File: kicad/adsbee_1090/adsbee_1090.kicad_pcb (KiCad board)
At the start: 4 copper layers, 33.5 x 30 mm, 84 parts, among them J1 U.FL 6GHz 50R, J2 USB_Micro-B_Receptacle, J3 Conn_02x03_Odd_Even, J4 Conn_ARM_JTAG_SWD_10, Q1 BSS84, SW1 SW_Push, SW2 SW_Push, SW3 SN74LVC1G3157, U1 AD8314, U2 BGA2818, U3 MCP6566, U4 AP2112K-3.3, U5 W25Q128JVS, U6 RP2040, U7 OPA358AIDCKR, X1 SF2321D, Y1 12.000MHz 18pF ±20ppm 80R

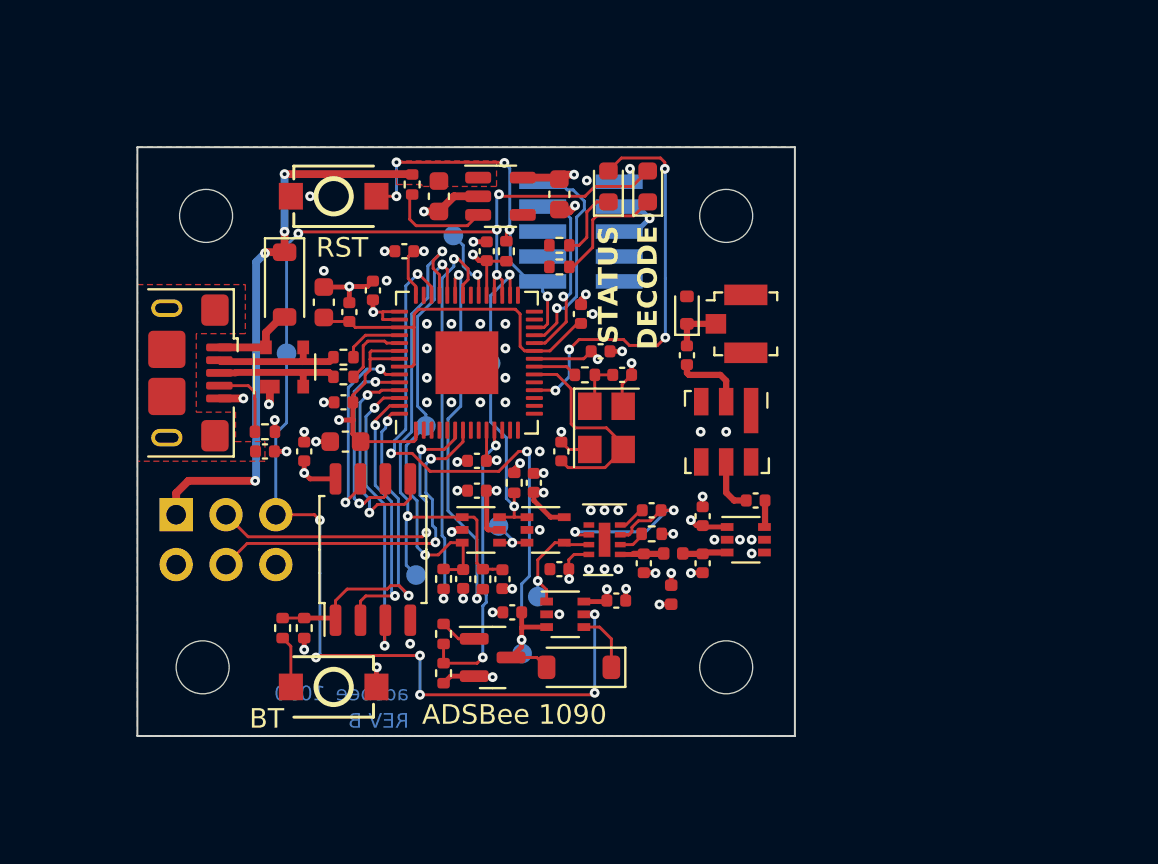
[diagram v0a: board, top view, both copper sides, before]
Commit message: Make ADSBee PCBA Rev C
* production folder for JLCPCB has U5 and X1 removed due to stockout.
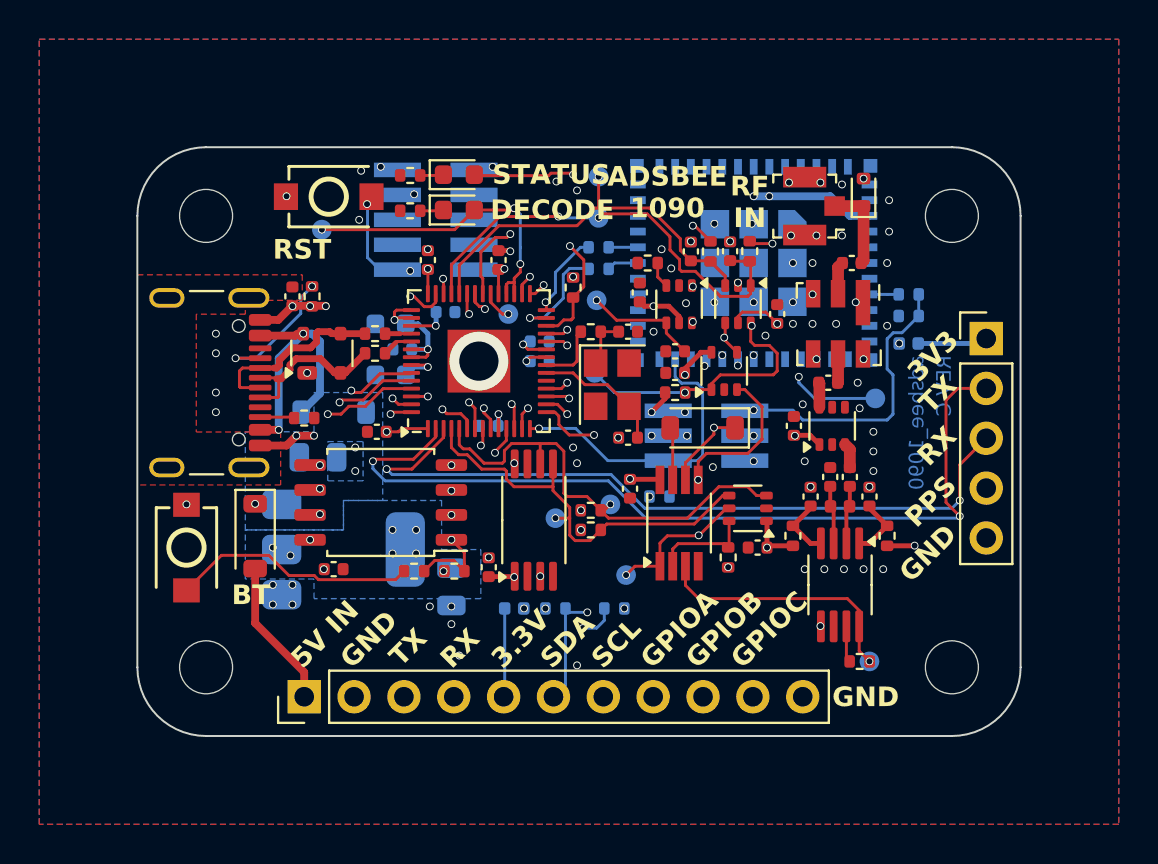
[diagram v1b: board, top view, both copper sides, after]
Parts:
- removed the C21 at (56.5, 37.9)
- removed the C27 at (60.8, 56.7)
- removed the C28 at (59.4, 58.6)
- removed the C8 at (61.2, 54.0)
- removed L2: 12nH, Inductor_SMD:L_0402_1005Metric
- removed Q1: BSS84, Package_TO_SOT_SMD:SOT-23
- removed the R13 at (49.0, 37.4)
- removed the R6 at (50.6, 60.3)
- removed the U1 at (58.8, 55.5)
- removed the U7 at (56.8, 59.3)
- added C10: 3pF, Capacitor_SMD:C_0402_1005Metric, F.Cu at (70.3, 52.3)
- added C13: 0.1uF, Capacitor_SMD:C_0402_1005Metric, F.Cu at (66.6, 55.9)
- added C14: 0.1uF, Capacitor_SMD:C_0402_1005Metric, F.Cu at (60.6, 42.9)
- added C32: 10uF, Capacitor_SMD:C_0805_2012Metric, B.Cu at (51.0, 57.9)
- added C4: 0.1uF, Capacitor_SMD:C_0402_1005Metric, F.Cu at (69.3, 53.3)
- added C6: 0.1uF, Capacitor_SMD:C_0402_1005Metric, F.Cu at (60.1, 52.9)
- added C9: 3pF, Capacitor_SMD:C_0402_1005Metric, F.Cu at (71.3, 52.3)
- added D6: 20V 1A, Diode_SMD:D_SOD-123, F.Cu at (41.0, 55.3)
- added F1: 6V 200mA, Fuse:Fuse_0402_1005Metric, B.Cu at (74.3, 45.5)
- added F2: 6V 200mA, Fuse:Fuse_0402_1005Metric, B.Cu at (54.2, 59.0)
- added J5: Conn_01x05_Pin, Connector_PinHeader_2.54mm:PinHeader_1x05_P2.54mm_Vertical, F.Cu at (78.2, 45.2)
- added J6: Conn_01x11_Pin, Connector_PinHeader_2.54mm:PinHeader_1x11_P2.54mm_Vertical, F.Cu at (43.5, 63.5)
- added R10: 5.1k, Resistor_SMD:R_0402_1005Metric, F.Cu at (43.5, 49.3)
- added R11: 2.2k, Resistor_SMD:R_0402_1005Metric, F.Cu at (58.1, 55.0)
- added R12: 2.2k, Resistor_SMD:R_0402_1005Metric, F.Cu at (58.1, 54.0)
- added R16: 2.2k, Resistor_SMD:R_0402_1005Metric, B.Cu at (56.3, 59.0)
- added R17: 2.2k, Resistor_SMD:R_0402_1005Metric, B.Cu at (59.3, 59.0)
- added R18: 0R, Resistor_SMD:R_0402_1005Metric, B.Cu at (74.3, 43.0)
- added R19: 0R, Resistor_SMD:R_0402_1005Metric, B.Cu at (58.5, 40.6)
- added R2: 10R, Resistor_SMD:R_0402_1005Metric, F.Cu at (73.2, 55.3)
- added R20: 0R, Resistor_SMD:R_0402_1005Metric, B.Cu at (58.5, 41.7)
- added R22: 10k, Resistor_SMD:R_0402_1005Metric, B.Cu at (61.6, 53.3)
- added R23: 10k, Resistor_SMD:R_0402_1005Metric, B.Cu at (74.3, 44.1)
- added R8: 20R, Resistor_SMD:R_0402_1005Metric, F.Cu at (61.0, 41.4)
- added R9: 5.1k, Resistor_SMD:R_0402_1005Metric, F.Cu at (43.9, 43.1)
- added SW2: SN74LVC1G3157, Package_TO_SOT_SMD:SOT-363_SC-70-6, F.Cu at (62.6, 43.5)
- added TP3: TestPoint, TestPoint:TestPoint_Pad_D1.0mm, B.Cu at (72.3, 61.7)
- added TP6: TestPoint, TestPoint:TestPoint_Pad_D1.0mm, B.Cu at (59.1, 53.7)
- added TP7: TestPoint, TestPoint:TestPoint_Pad_D1.0mm, B.Cu at (56.3, 54.4)
- added U10: AMS1117-3.3, Package_TO_SOT_SMD:SOT-223-3_TabPin2, B.Cu at (45.5, 56.0)
- added U2: AD8313xRM, Package_SO:MSOP-8_3x3mm_P0.65mm, F.Cu at (70.8, 57.8)
- added U3: TLV3542, Package_SO:VSSOP-8_3.0x3.0mm_P0.65mm, F.Cu at (62.6, 54.6)
- added U6: M24C02-RDW, Package_SO:TSSOP-8_4.4x3mm_P0.65mm, F.Cu at (55.2, 54.5)
- added U9: ESP32-PICO-MINI-02U, Custom_MCU_Espressif:ESP32-PICO-MINI-02U, B.Cu at (66.4, 41.4)
- C16: renamed from C10; moved to B.Cu
- C17: renamed from C11; moved to B.Cu
- C21: renamed from C15; moved to B.Cu
- C22: renamed from C16; moved to B.Cu
- C23: renamed from C17; moved to B.Cu
- C24: renamed from C18; moved to B.Cu
- C25: renamed from C19; moved to B.Cu
- C26: value 7pF -> 0.1uF
- C31: renamed from C22; value 1uF -> 10uF; footprint Capacitor_SMD:C_0603_1608Metric -> Capacitor_SMD:C_0805_2012Metric; moved to B.Cu
- D3: renamed from D2; moved to B.Cu
- J2: value USB_Micro-B_Receptacle -> USB_C_Receptacle_USB2.0_16P; footprint Custom_Connector_USB:USB_Micro-B_Amphenol_10118193-0001LF_Horizontal -> Custom_Connector_USB:USB_C_Receptacle_GCT_USB4105-xx-A_16P_TopMnt_Horizontal
- J3: value Conn_02x03_Odd_Even -> Conn_02x03_Pin; footprint Connector_PinHeader_2.54mm:PinHeader_2x03_P2.54mm_Vertical -> Connector_PinHeader_1.27mm:PinHeader_2x03_P1.27mm_Vertical_SMD
- L1: value 100nH -> 8.2nH RF
- R3: value 10k -> 10R
- R5: value 10k -> 0R
- R7: value 5.1k -> 1k
- U4: value AP2112K-3.3 -> MCP4017-104E 100k; footprint Package_TO_SOT_SMD:SOT-23-5 -> Package_TO_SOT_SMD:SOT-363_SC-70-6
- moved PCB1 34.1 mm to (76.9, 46.1), turned to -90 degrees
- moved J3 27.3 mm to (64.0, 50.2), turned to 180 degrees
- moved R7 24.5 mm to (65.1, 56.4), turned to -90 degrees
- moved R4 21.5 mm to (66.2, 40.8), turned to 90 degrees
- moved R1 21.5 mm to (64.2, 40.8), turned to 90 degrees
- moved R5 21.2 mm to (71.8, 61.7), turned to 0 degrees
- moved TP4 20.4 mm to (58.5, 39.1)
- moved C11 20.3 mm to (65.2, 40.8), turned to 90 degrees
- moved C1 20.3 mm to (63.2, 40.8), turned to 90 degrees
- moved U4 20.3 mm to (66.1, 53.9), turned to 180 degrees
- moved TP2 20.3 mm to (72.6, 48.3)
- moved TP8 18.4 mm to (58.4, 43.3)
- moved C5 17.8 mm to (67.6, 44.0), turned to 90 degrees
- moved SW1 17.4 mm to (65.6, 43.5), turned to -90 degrees
- moved C3 16.2 mm to (72.3, 53.3), turned to -90 degrees
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- renumbered C9 to C1, C2 to C11, C4 to C12, C29 to C15, C12 to C18, C13 to C19, C1 to C2, C14 to C20, C20 to C27, C23 to C28, C24 to C29, C25 to C30, C7 to C5, C5 to C7, C6 to C8, D5 to D2, D3 to D4, D4 to D5, R2 to R1, R10 to R13, R11 to R14, R12 to R15, R14 to R21, R15 to R24, R16 to R25, R8 to R26, R9 to R27, R1 to R4, R4 to R6, SW3 to SW1, SW1 to SW3, SW2 to SW4, TP3 to TP1, TP5 to TP10, TP7 to TP11, TP1 to TP2, TP6 to TP4, TP2 to TP5, TP4 to TP9, U2 to U1, U3 to U5, U5 to U7, U6 to U8
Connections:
- C15 pad 1: /RSSI_HOLD -> GND
- C15 pad 2: +3V3 -> /RSSI_HOLD
- C26 pad 1: /RF_DET_IN -> GND
- C26 pad 2: GND -> +3V3
- C3 pad 2: /3V3_FILT_RF_DET -> Net-(C3-Pad2)
- D2 pad 1: Net-(D5-K) (its old number) -> /RSSI_PEAK
- D2 pad 2: /RSSI_HOLD -> Net-(D2-A)
- J3 pad 1: +5V -> /ESP32_ENABLE
- J3 pad 2: GND -> +3V3
- J3 pad 3: /UART_TX -> /ESP32_UART0_RX
- J3 pad 4: /UART_RX -> GND
- J3 pad 5: /DECODE -> /ESP32_UART0_TX
- J3 pad 6: GND -> /ESP32_GPIO0_BOOT
- L1 pad 1: /3V3_FILT_RF_DET -> /RF_DET_IN+
- L1 pad 2: +3V3 -> /RF_DET_IN-
- R3 pad 1: /3V3_FILT_RF_DET -> +3V3
- R5 pad 1: /~{RSSI_CLEAR} -> Net-(U2-VSET)
- R5 pad 2: +3V3 -> /RF_DET_OUT
- R7 pad 1: Net-(J2-ID) -> Net-(U3A--)
- TP5 pad 1: /RF_DET_OUT -> /RF_LEVEL
- U1 pad 3: /RF_DET_IN -> Net-(C9-Pad1)
- U4 pad 1: +5V -> +3V3
- U4 pad 3: Net-(U4-EN) -> /I2C1_SCL
- U4 pad 4: unconnected-(U4-NC-Pad4) -> /I2C1_SDA
- U4 pad 5: +3V3 -> /RF_LEVEL
- U5 pad 3: /MTL_BIAS -> /RF_LEVEL
- U5 pad 4: /RF_DET_OUT -> /MTL_BIAS
- U8 pad 11: /~{RSSI_CLEAR} -> /ESP32_SPI_MOSI
- U8 pad 12: unconnected-(U6-GPIO9-Pad12) -> /ESP32_SPI_MISO
- U8 pad 13: unconnected-(U6-GPIO10-Pad13) -> /ESP32_SPI_CS
- U8 pad 14: unconnected-(U6-GPIO11-Pad14) -> /ESP32_GPIO0_BOOT
- U8 pad 15: unconnected-(U6-GPIO12-Pad15) -> /I2C0_SDA
- U8 pad 16: unconnected-(U6-GPIO13-Pad16) -> /I2C0_SCL
- U8 pad 17: unconnected-(U6-GPIO14-Pad17) -> /ESP32_ENABLE
- U8 pad 2: unconnected-(U6-GPIO0-Pad2) -> /GNSS_UART0_TX
- U8 pad 27: unconnected-(U6-GPIO16-Pad27) -> /ESP32_UART0_TX
- U8 pad 28: unconnected-(U6-GPIO17-Pad28) -> /ESP32_UART0_RX
- U8 pad 29: unconnected-(U6-GPIO18-Pad29) -> /AUX_GPIOA
- U8 pad 3: unconnected-(U6-GPIO1-Pad3) -> /GNSS_UART0_RX
- U8 pad 35: unconnected-(U6-GPIO23-Pad35) -> /AUX_GPIOB
- U8 pad 4: unconnected-(U6-GPIO2-Pad4) -> /I2C1_SDA
- U8 pad 41: unconnected-(U6-GPIO29_ADC3-Pad41) -> /AUX_GPIOC
- U8 pad 5: unconnected-(U6-GPIO3-Pad5) -> /I2C1_SCL
- U8 pad 6: /UART_TX -> /UART1_TX
- U8 pad 7: /UART_RX -> /UART1_RX
- U8 pad 8: unconnected-(U6-GPIO6-Pad8) -> /GNSS_PPS
- U8 pad 9: unconnected-(U6-GPIO7-Pad9) -> /ESP32_SPI_CLK
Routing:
- net /GNSS_UART0_TX: track 0.00 -> 44.0 mm, vias 0 -> 2
- net /DECODE: track 69.8 -> 27.0 mm, vias 10 -> 5
- net /GNSS_UART0_RX: track 0.00 -> 37.9 mm, vias 0 -> 2
- net /AUX_GPIOC: track 0.00 -> 37.5 mm, vias 0 -> 2
- net /AUX_GPIOB: track 0.00 -> 35.8 mm, vias 0 -> 2
- net /GNSS_PPS: track 0.00 -> 28.6 mm, vias 0 -> 1
- net +5V: track 28.5 -> 0.00 mm, vias 4 -> 1
- net /AUX_GPIOA: track 0.00 -> 26.1 mm, vias 0 -> 2
- net /ESP32_ENABLE: track 0.00 -> 25.4 mm, vias 0 -> 2
- net /ESP32_UART0_TX: track 0.00 -> 23.4 mm, vias 0 -> 3
- net /I2C1_SCL: track 0.00 -> 22.9 mm, vias 0 -> 1
- net GND: track 29.7 -> 7.22 mm, vias 61 -> 77
- net /ESP32_UART0_RX: track 0.00 -> 21.8 mm, vias 0 -> 3
- net /I2C1_SDA: track 0.00 -> 21.1 mm, vias 0 -> 1
- net /RSSI_HOLD: track 35.2 -> 14.9 mm, vias 4 -> 2
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- added copper zone on B.Cu, net +3V3
- added copper zone on In4.Cu, net +3V3
- added copper zone on B.Cu, net +5V
- added copper zone on In4.Cu, net GND
- removed copper zone on In2.Cu, net +3V3
- removed copper zone on F.Cu, net +5V
- removed copper zone on In2.Cu, net /3V3_FILT_RF_DET
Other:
- board size 33.5 x 30 mm -> 45 x 30 mm
- copper layers 4 -> 6
- board text added: "0.0000 mm / 0.0000 mm"
- board text added: "0.0152 mm"
- board text added: "0.1500 mm"
- board text added: "0.2028 mm"
- board text added: "0.2104 mm"
- board text added: "0.4 mm"
- board text added: "1.5844 mm"
- board text added: "131.9816 mm x 52.3267 mm"
- board text added: "3.3V"
- board text added: "3V3"
- board text added: "5V IN"
- board text added: "6"
- board text added: "ADSBEE 1090"
- board text added: "BOARD CHARACTERISTICS"
- board text added: "Board Thickness:"
- board text added: "Board overall dimensions:"
- board text added: "Castellated pads:"
- board text added: "Copper Finish:"
- board text added: "Copper Layer Count:"
- board text added: "Dielectric 4"
- board text added: "Dielectric 5"
- board text added: "ENABLE"
- board text added: "ENIG"
- board text added: "Edge card connectors:"
- board text added: "GPIO0_BOOT"
- board text added: "GPIOA"
- board text added: "GPIOB"
- board text added: "GPIOC"
- board text added: "I2C1_SCL"
- board text added: "I2C1_SDA"
- board text added: "Impedance Control:"
- board text added: "In3.Cu"
- board text added: "In4.Cu"
- board text added: "Min hole diameter:"
- board text added: "Min track/spacing:"
- board text added: "No"
- board text added: "PPS"
- board text added: "Plated Board Edge:"
- board text added: "RF IN"
- board text added: "RF_LEVEL"
- board text added: "RX"
- board text added: "SCL"
- board text added: "SDA"
- board text added: "TX"
- board text added: "UART0_RX"
- board text added: "UART0_TX"
- board text added: "White"
- board text added: "pantsforbirds.com"
- board text removed: "+5V"
- board text removed: "0.03 mm"
- board text removed: "0.203 mm"
- board text removed: "1.03 mm"
- board text removed: "ADSBee 1090"
- board text removed: "UART_RX"
- board text removed: "UART_TX"
- board text removed: "Yellow"

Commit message: Change drawing notes and add iBOM export
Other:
- board text added: "0.3000 mm"
- board text added: "45.0000 mm x 30.0000 mm"
- board text removed: "0.1500 mm"
- board text removed: "131.9816 mm x 52.3267 mm"
